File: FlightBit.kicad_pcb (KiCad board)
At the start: 4 copper layers, 40 x 40 mm, 61 parts, among them J1 SBUS, J2 USB_C_Receptacle_USB2.0, J3 PPM, J4 OUT, J5 Conn_01x02, J6 Conn_01x02, Q1 1P, SW1 SW_Push, U1 STM32F103C8Tx, U2 MPU-6050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

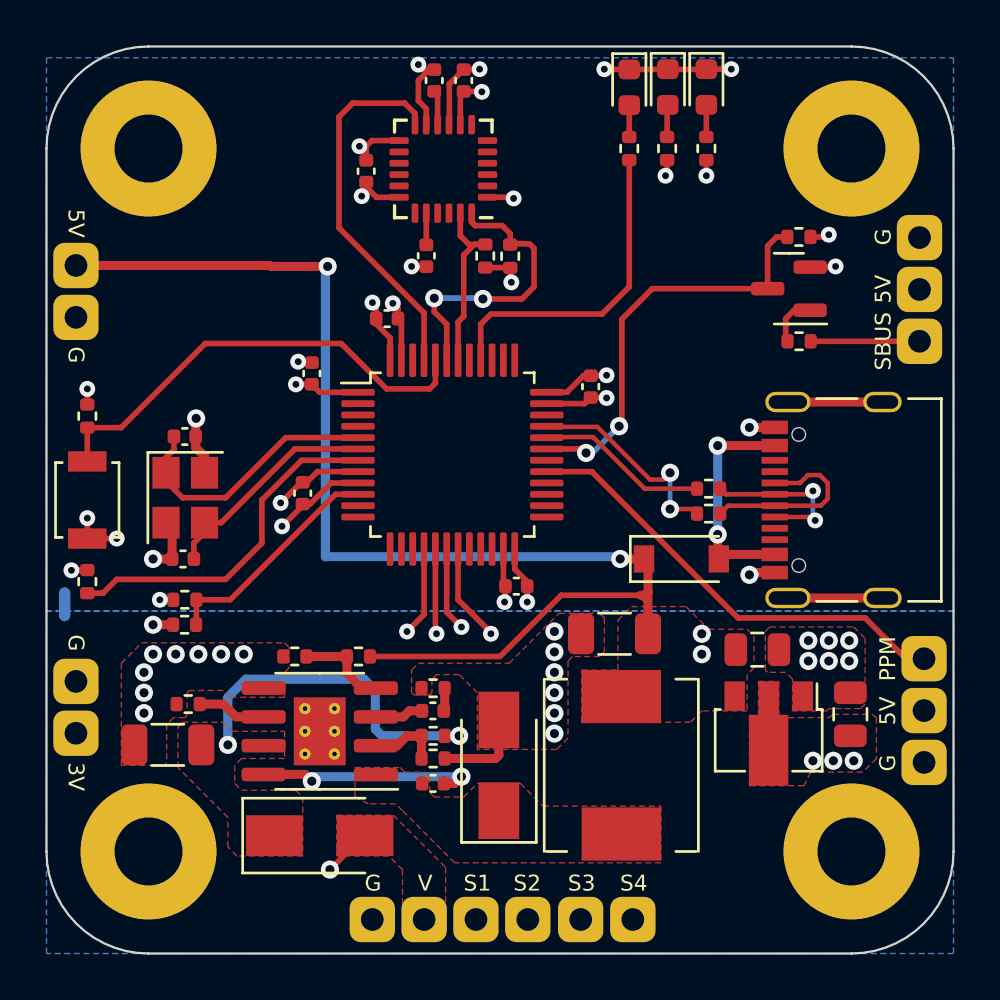
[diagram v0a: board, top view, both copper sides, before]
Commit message: add debug connector
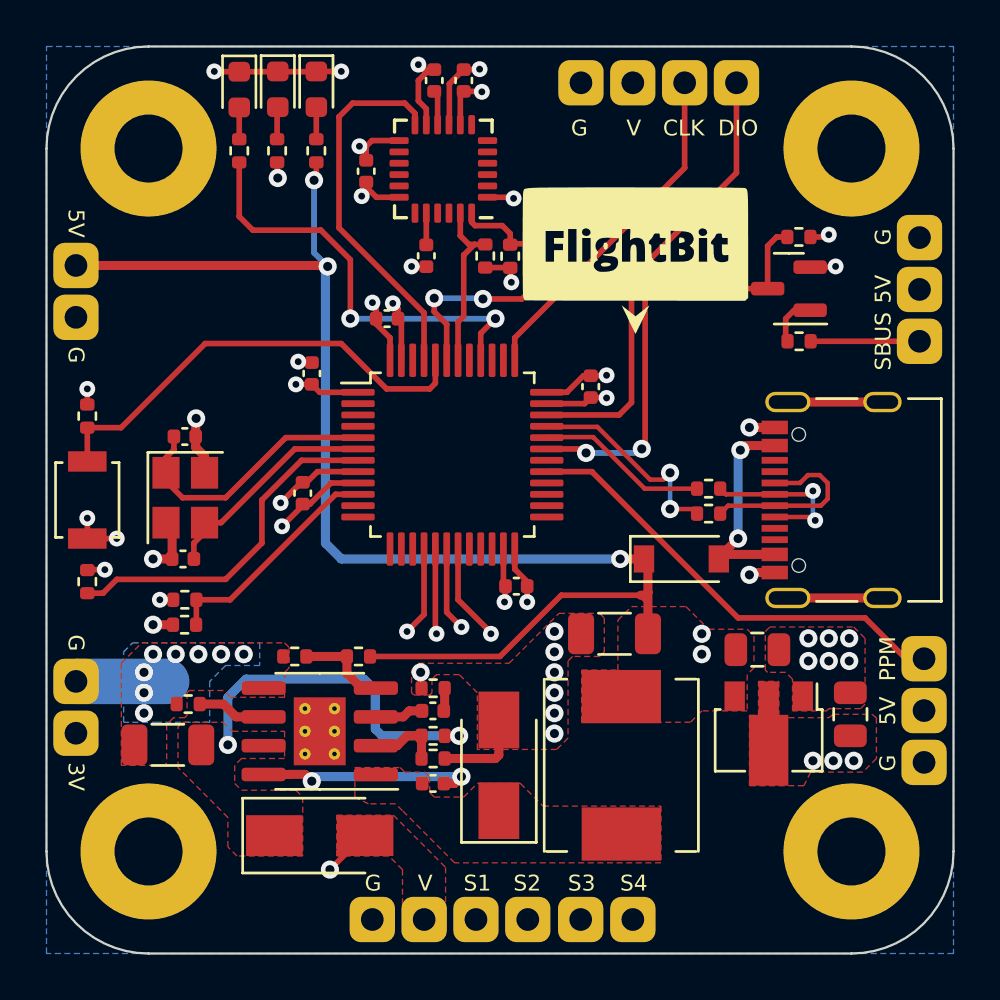
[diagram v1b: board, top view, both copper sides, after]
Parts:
- added G***: LOGO, SFA_LOGO:Arrow, F.Cu at (145.7, 89.3)
- added G***: LOGO, SFA_LOGO:FlightBit, F.Cu at (145.7, 85.9)
- added J7: Conn_01x04, myCustomLibs:pad_01x04, F.Cu at (143.3, 78.8)
- NT1: footprint NetTie:NetTie-2_SMD_Pad0.5mm -> NetTie:NetTie-2_SMD_Pad2.0mm
- moved D3 17.2 mm to (128.2, 79.1)
- moved D5 17.2 mm to (131.6, 79.1)
- moved R15 17.2 mm to (128.2, 81.8)
- moved R17 17.2 mm to (131.6, 81.8)
- moved D4 17.2 mm to (129.9, 79.1)
- moved R16 17.2 mm to (129.9, 81.8)
- moved NT1 4.22 mm to (123.0, 105.2), turned to 180 degrees
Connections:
- U1 pad 34: unconnected-(U1-Pad34) -> /SWDIO
- U1 pad 37: unconnected-(U1-Pad37) -> /SWCLK
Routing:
- net /SWDIO: track 0.00 -> 20.0 mm
- net /SWCLK: track 0.00 -> 15.3 mm
- net /LED_STATUS: track 14.4 -> 19.2 mm, vias 0 -> 2
- net +5V: track 99.3 -> 97.4 mm
- net /UART1_RX: track 18.4 -> 19.6 mm
- net VBUS: track 10.1 -> 9.34 mm
- net GNDPWR: vias 14 -> 15
- added copper zone on In2.Cu, net +3V3
- added copper zone on In1.Cu, net GND
- added copper zone on In1.Cu, net GNDPWR
- removed copper zone on In1.Cu, net +3V3
- removed copper zone on In2.Cu, net GND
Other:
- board text added: "CLK"
- board text added: "DIO"
